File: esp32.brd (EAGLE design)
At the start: 123.5 x 80.4 mm, 21 parts, among them IC1 LM1117IMPX-3.3, U1 ESP32MOD

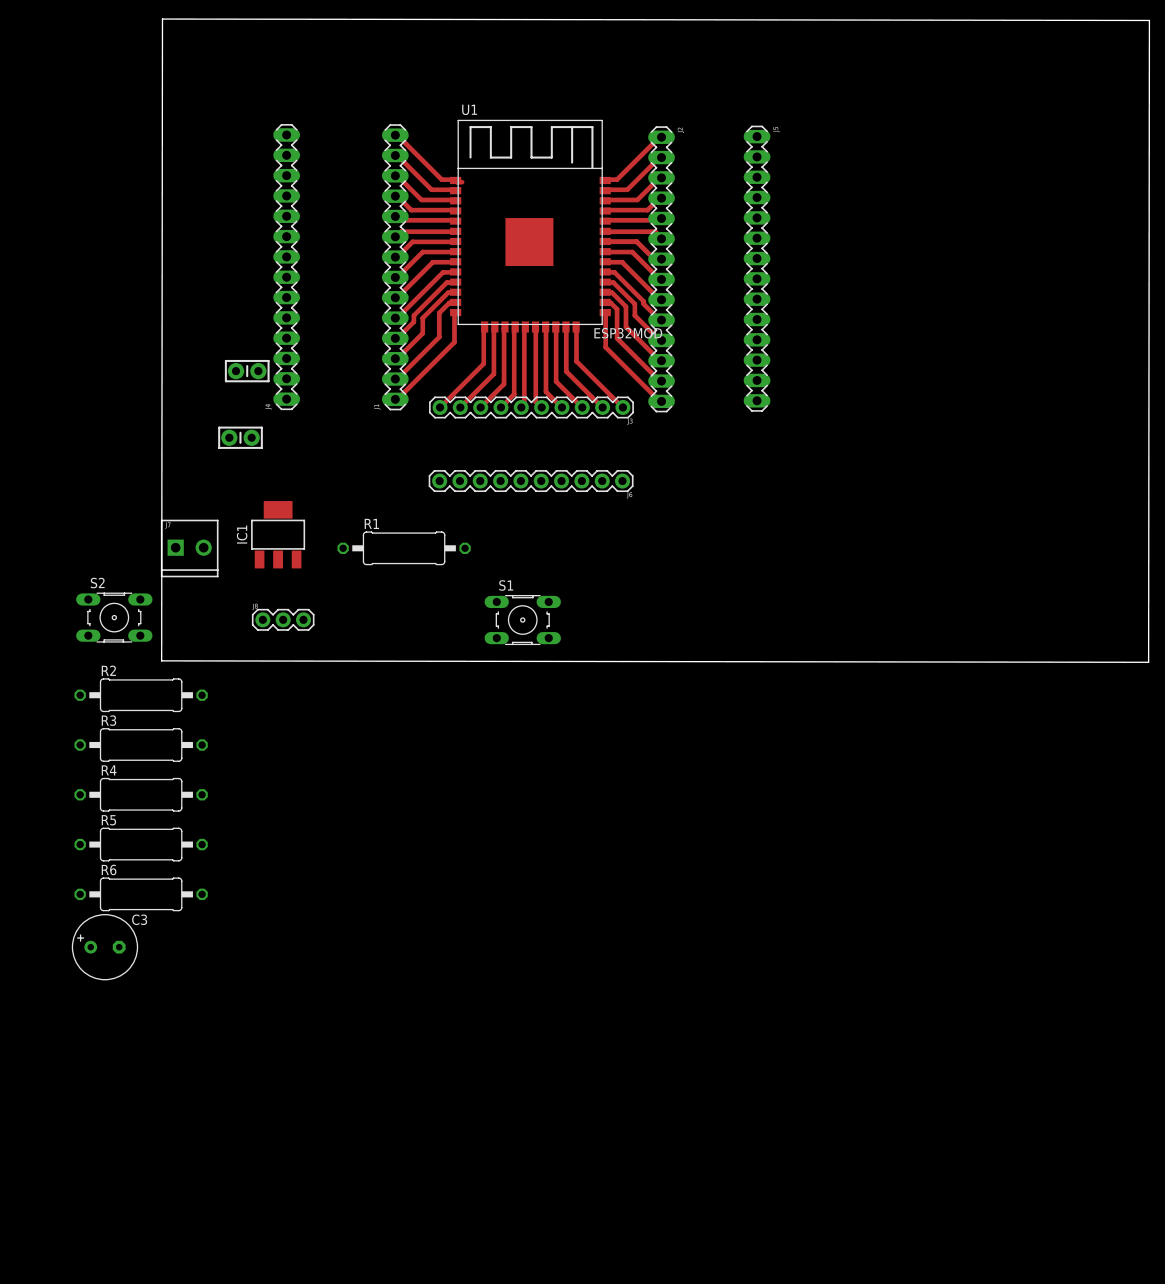
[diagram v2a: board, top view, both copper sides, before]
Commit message: Added LEDs and improved reset circuitry
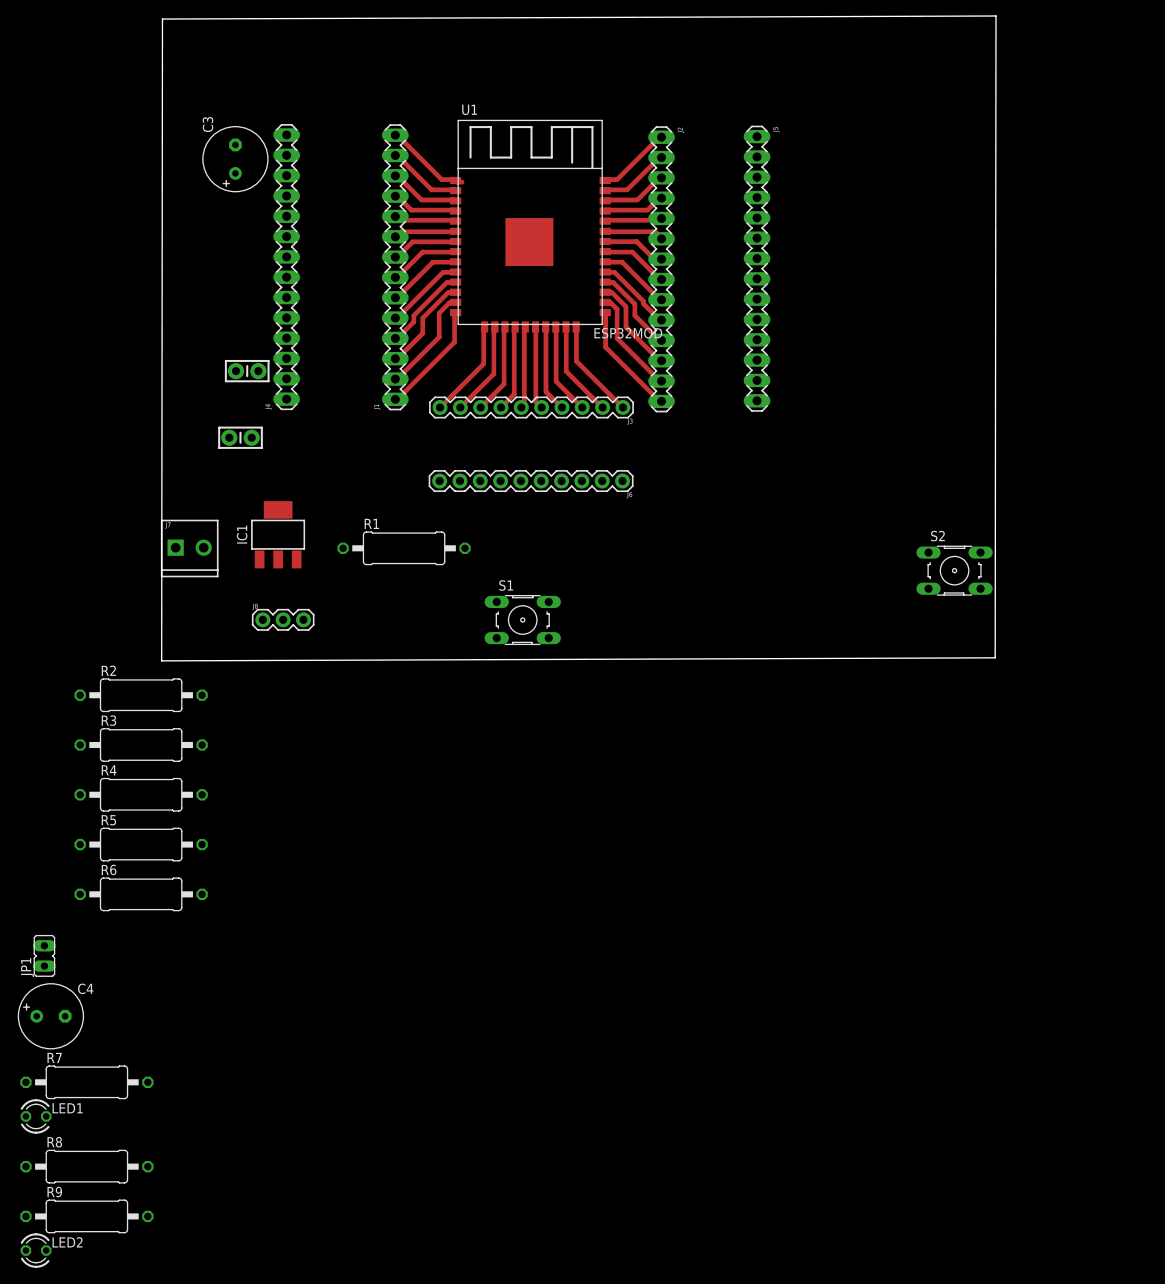
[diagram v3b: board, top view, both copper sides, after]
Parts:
- added C4: (no value), rcl:E3,5-8
- added JP1: (no value), jumper:JP1
- added LED1, LED2: TLLY4400, led:LED3MM
- added R7: 4.7k, rcl:0411/15
- added R8, R9: 330, rcl:0411/15
- moved S2 105.2 mm to (97.6, 23.0)
- moved C3 99.8 mm to (7.70, 74.5), turned to 90 degrees
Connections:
- removed net N$18: J2.2, J5.2, U1.37
- new net LED: J2.2, J5.2, JP1.1, LED2.A, U1.37
- new net N$4: LED1.K, R8.1
- new net N$5: LED2.K, R9.1
- new net RST_TRIGGER: C4.-, JP1.2, R7.2, S1.1, S1.2
- net 3.3V: now also LED1.A, R7.1
- net GND: now also R8.2, R9.2
- net RST: now also C4.+; no longer S1.1, S1.2
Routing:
- net N$18: track 8.81 -> 0.00 mm
- net LED: track 0.00 -> 8.69 mm
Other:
- board size 123.5 x 80.4 mm -> 104.3 x 80.6 mm

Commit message: Finalized the layout with cheap design
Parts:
- removed R2, R3, R4, R5, R6: 4.7k, rcl:0411/15
- removed U1: ESP32MOD, ESP3x:ESP32MOD
- added J10, J11: (no value), SparkFun-Connectors:1X14-LONGPADS
- added J12: (no value), SparkFun-Connectors:1X10
- added J9: (no value), SparkFun-Connectors:1X03
- added R10: 330, rcl:0207/12
- added R11, R12, R13, R14: 4.7k, rcl:0207/12
- R1, R7, R8: device rcl:0411/15 -> rcl:0207/12
- R9: value 330 -> 4.7k; device rcl:0411/15 -> rcl:0207/12
- moved LED2 166.9 mm to (78.2, 74.9), turned to 90 degrees
- moved R8 147.1 mm to (73.9, 68.8), turned to 90 degrees
- moved LED1 138.9 mm to (81.5, 52.6), turned to 180 degrees
- moved R9 131.4 mm to (40.3, 63.3), turned to 90 degrees
- moved R7 102.9 mm to (61.1, 32.6), turned to 270 degrees
- moved S2 90.0 mm to (8.16, 33.3), turned to 270 degrees
- moved JP1 86.6 mm to (6.15, 58.5), turned to 90 degrees
- moved C4 84.3 mm to (9.38, 47.9), turned to 180 degrees
- moved C3 76.7 mm to (75.5, 38.6)
- moved C2 60.8 mm to (69.1, 38.9), turned to 270 degrees
- moved S1 60.6 mm to (7.86, 65.8), turned to 90 degrees
- moved IC1 54.0 mm to (66.9, 31.5), flipped to the bottom, turned to 90 degrees
- moved C1 42.9 mm to (48.1, 29.9), turned to 90 degrees
- moved J8 31.2 mm to (40.9, 26.2), turned to 90 degrees
- moved J7 30.6 mm to (30.7, 28.6)
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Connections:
- net 3.3V: now also J10.13, R11.2, R13.1, R14.1, R9.2; no longer R1.1, R2.2, R5.1, R6.2, U1.2
- net GND: now also J10.14, J11.1, J12.10, J9.1, R1.1, R10.1, R12.1, R8.1; no longer R3.2, R4.1, R8.2, R9.2, U1.0, U1.1, U1.15, U1.38
- net LED: now also J11.2; no longer U1.37
- net N$1: now also J11.7; no longer U1.32
- net N$10: now also J10.5; no longer U1.10
- net N$11: now also J10.4; no longer U1.11
- net N$12: now also J10.3; no longer U1.12
- net N$13: now also J10.2; no longer U1.13
- net N$14: now also J10.1, R1.2; no longer R4.2, U1.14
- net N$15: now also J11.5, J9.3; no longer U1.34
- net N$16: now also J11.4, J9.2; no longer U1.35
- net N$17: now also J11.3; no longer U1.36
- net N$19: now also J11.10, R14.2; no longer R6.1, U1.29
- net N$2: now also J10.11; no longer U1.4
- net N$20: now also J11.6; no longer U1.33
- net N$22: now also J11.8; no longer U1.31
- net N$23: now also J11.9; no longer U1.30
- net N$25: now also J11.11; no longer U1.28
- net N$26: now also J11.12; no longer U1.27
- net N$27: now also J11.13; no longer U1.26
- net N$28: now also J11.14, R13.2; no longer R2.1, U1.25
- net N$3: now also J10.10; no longer U1.5
- net N$30: now also J12.9; no longer U1.16
- net N$31: now also J12.8; no longer U1.17
- net N$32: now also J12.7; no longer U1.18
- net N$33: now also J12.6; no longer U1.19
- net N$34: now also J12.5; no longer U1.20
- net N$35: now also J12.4; no longer U1.21
- net N$36: now also J12.3; no longer U1.22
- net N$37: now also J12.2, R7.2; no longer R5.2, U1.23
- net N$38: now also J12.1, R12.2; no longer R3.1, U1.24
- net N$4: now also R10.2; no longer R8.1
- net N$5: now also R8.2; no longer R9.1
- net N$6: now also J10.9; no longer U1.6
- net N$7: now also J10.8; no longer U1.7
- net N$8: now also J10.7; no longer U1.8
- net N$9: now also J10.6; no longer U1.9
- net RST: now also J10.12, R9.1; no longer R1.2, U1.3
- net RST_TRIGGER: now also R11.1; no longer R7.2
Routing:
- net 3.3V: track 9.35 -> 136.2 mm, vias 0 -> 1
- net N$28: track 14.2 -> 94.4 mm
- net LED: track 8.69 -> 86.8 mm
- net RST: track 8.82 -> 57.9 mm
- net 5V: track 0.00 -> 44.2 mm, vias 0 -> 2
- net RST_TRIGGER: track 0.00 -> 29.6 mm
- net N$19: track 9.77 -> 35.5 mm
- net GND: track 33.4 -> 11.9 mm, vias 0 -> 2
- net N$15: track 7.23 -> 22.2 mm
- net N$16: track 7.76 -> 22.2 mm
- net N$37: track 12.0 -> 25.5 mm, vias 0 -> 2
- net N$42: track 0.00 -> 10.5 mm
- net N$13: track 13.3 -> 7.09 mm
- net N$30: track 11.8 -> 6.19 mm
- net N$36: track 11.4 -> 6.19 mm
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- added copper zone on layer 16, net 3.3V
- added copper zone on layer 16, net GND
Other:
- board size 104.3 x 80.6 mm -> 87.8 x 59.6 mm
